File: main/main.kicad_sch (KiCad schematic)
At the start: 3 parts, among them SW1 SW_DPST_x2

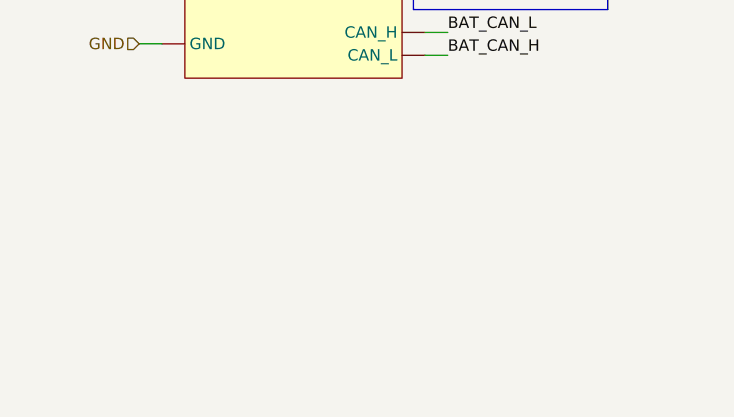
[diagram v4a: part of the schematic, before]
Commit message: Added motor, smart shunt, emergency switch and symbol of Cerbo GX
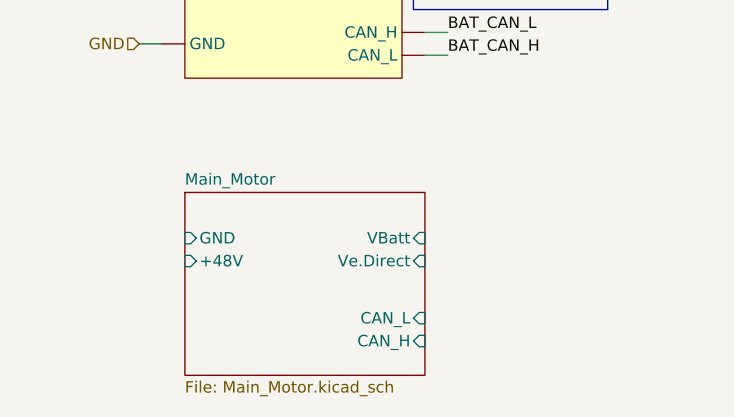
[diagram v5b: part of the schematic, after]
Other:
- added sheet Main_Motor (Main_Motor.kicad_sch)
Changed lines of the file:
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@@
+	)
+	(sheet
+		(at 29.21 125.73)
+		(size 26.67 20.32)
+		(fields_autoplaced yes)
+		(stroke
+			(width 0.1524)
+			(type solid)
+		)
+		(fill
+			(color 0 0 0 0.0000)
+		)
+		(property "Sheetname" "Main_Motor"
+			(at 29.21 125.0184 0)
+			(effects
+				(font
+					(size 1.27 1.27)
+				)
+				(justify left bottom)
+			)
+		)
+		(property "Sheetfile" "Main_Motor.kicad_sch"
+			(at 29.21 146.6346 0)
+			(effects
+				(font
+					(size 1.27 1.27)
+				)
+				(justify left top)
+			)
+		)
+		(pin "GND" input
+			(at 29.21 130.81 180)
+			(effects
+				(font
+					(size 1.27 1.27)
+				)
+				(justify left)
+			)
+		)
+		(pin "+48V" input
+			(at 29.21 133.35 180)
+			(effects
+				(font
+					(size 1.27 1.27)
+				)
+				(justify left)
+			)
+		)
+		(pin "VBatt" input
+			(at 55.88 130.81 0)
+			(effects
+				(font
+					(size 1.27 1.27)
+				)
+				(justify right)
+			)
+		)
+		(pin "Ve.Direct" input
+			(at 55.88 133.35 0)
+			(effects
+				(font
+					(size 1.27 1.27)
+				)
+				(justify right)
+			)
+		)
+		(pin "CAN_L" input
+			(at 55.88 139.7 0)
+			(effects
+				(font
+					(size 1.27 1.27)
+				)
+				(justify right)
+			)
+		)
+		(pin "CAN_H" input
+			(at 55.88 142.24 0)
+			(effects
+				(font
+					(size 1.27 1.27)
+				)
+				(justify right)
+			)
+		)
+		(instances
+			(project "main"
+				(path "/54fbbba9-a737-4199-9a4b-f9fa49b3de5e"
+					(page "20")
+				)
+			)
+		)
 	)
 	(sheet

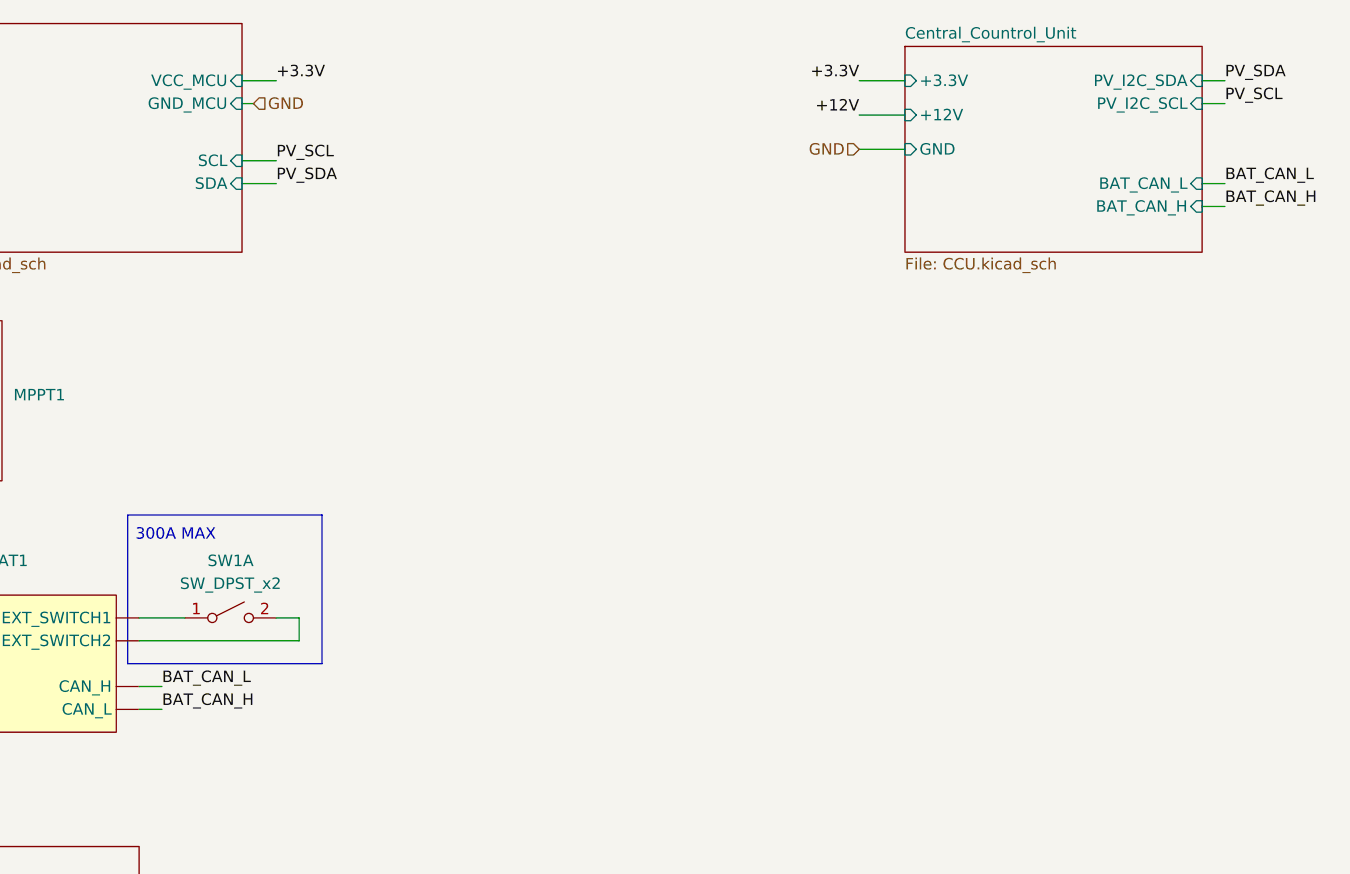
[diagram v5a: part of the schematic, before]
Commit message: Added sensors
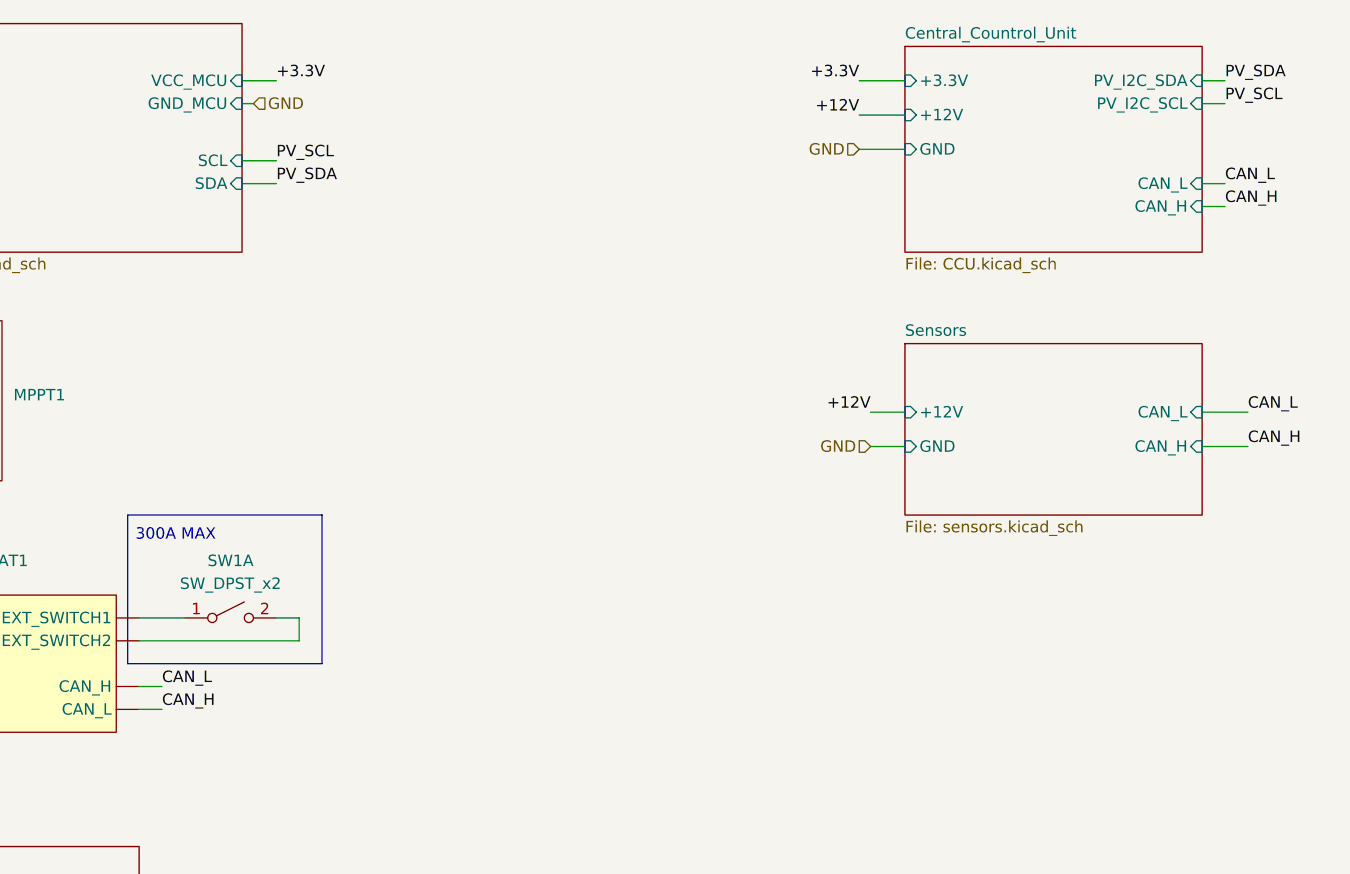
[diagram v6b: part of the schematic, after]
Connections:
- net BAT_CAN_H is gone; now on net GND: BAT1. (GND)
- net BAT_CAN_L is gone; now on net GND: BAT1. (GND)
- new net CAN_H: BAT1. (GND)
- new net CAN_L: BAT1. (GND)
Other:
- added sheet Sensors (sensors.kicad_sch)
- sheet Central_Countrol_Unit ports: added CAN_H, CAN_L; removed BAT_CAN_H, BAT_CAN_L
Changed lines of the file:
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@@
+	(wire
+		(pts
+			(xy 173.99 81.28) (xy 179.07 81.28)
+		)
+		(stroke
+			(width 0)
+			(type default)
+		)
+	)
 	(wire
 		(pts
@@
 		(pts
 			(xy 24.13 102.87) (xy 26.67 102.87)
+		)
+		(stroke
+			(width 0)
+			(type default)
+		)
+	)
+	(wire
+		(pts
+			(xy 137.16 77.47) (xy 140.97 77.47)
+		)
+		(stroke
+			(width 0)
+			(type default)
+		)
+	)
+	(wire
+		(pts
+			(xy 137.16 81.28) (xy 140.97 81.28)
+		)
+		(stroke
+			(width 0)
+			(type default)
+		)
+	)
+	(wire
+		(pts
+			(xy 173.99 77.47) (xy 179.07 77.47)
 		)
 		(stroke
@@
 		)
 	)
-	(label "BAT_CAN_H"
+	(label "CAN_H"
 		(at 176.53 54.61 0)
 		(fields_autoplaced yes)
@@
 		)
 	)
-	(label "BAT_CAN_L"
+	(label "+12V"
+		(at 137.16 77.47 180)
+		(fields_autoplaced yes)
+		(effects
+			(font
+				(size 1.27 1.27)
+			)
+			(justify right bottom)
+		)
+	)
+	(label "CAN_L"
+		(at 179.07 77.47 0)
+		(fields_autoplaced yes)
+		(effects
+			(font
+				(size 1.27 1.27)
+			)
+			(justify left bottom)
+		)
+	)
+	(label "CAN_H"
+		(at 179.07 81.28 0)
+		(fields_autoplaced yes)
+		(effects
+			(font
+				(size 1.27 1.27)
+			)
+			(justify left bottom)
+		)
+	)
+	(label "CAN_L"
 		(at 176.53 52.07 0)
 		(fields_autoplaced yes)
@@
 		)
 	)
-	(label "BAT_CAN_H"
+	(label "CAN_H"
 		(at 58.42 110.49 0)
 		(fields_autoplaced yes)
@@
 		)
 	)
-	(label "BAT_CAN_L"
+	(label "CAN_L"
 		(at 58.42 107.95 0)
 		(fields_autoplaced yes)
@@
 		(shape input)
 		(at 22.86 72.39 180)
+		(fields_autoplaced yes)
+		(effects
+			(font
+				(size 1.27 1.27)
+			)
+			(justify right)
+		)
+	)
+	(hierarchical_label "GND"
+		(shape input)
+		(at 137.16 81.28 180)
 		(fields_autoplaced yes)
 		(effects
@@
 			)
 		)
-		(pin "BAT_CAN_L" input
+		(pin "CAN_L" input
 			(at 173.99 52.07 0)
 			(effects
@@
 			)
 		)
-		(pin "BAT_CAN_H" input
+		(pin "CAN_H" input
 			(at 173.99 54.61 0)
 			(effects
@@
 				)
 			)
+		)
+	)
+	(sheet
+		(at 140.97 69.85)
+		(size 33.02 19.05)
+		(fields_autoplaced yes)
+		(stroke
+			(width 0.1524)
+			(type solid)
+		)
+		(fill
+			(color 0 0 0 0.0000)
+		)
+		(property "Sheetname" "Sensors"
+			(at 140.97 69.1384 0)
+			(effects
+				(font
+					(size 1.27 1.27)
+				)
+				(justify left bottom)
+			)
+		)
+		(property "Sheetfile" "sensors.kicad_sch"
+			(at 140.97 89.4846 0)
+			(effects
+				(font
+					(size 1.27 1.27)
+				)
+				(justify left top)
+			)
+		)
+		(pin "CAN_H" input
+			(at 173.99 81.28 0)
+			(effects
+				(font
+					(size 1.27 1.27)
+				)
+				(justify right)
+			)
+		)
+		(pin "CAN_L" input
+			(at 173.99 77.47 0)
+			(effects
+				(font
+					(size 1.27 1.27)
+				)
+				(justify right)
+			)
+		)
+		(pin "+12V" input
+			(at 140.97 77.47 180)
+			(effects
+				(font
+					(size 1.27 1.27)
+				)
+				(justify left)
+			)
+		)
+		(pin "GND" input
+			(at 140.97 81.28 180)
+			(effects
+				(font
+					(size 1.27 1.27)
+				)
+				(justify left)
+			)
+		)
+		(instances
+			(project "main"
+				(path "/54fbbba9-a737-4199-9a4b-f9fa49b3de5e"
+					(page "21")
+				)
+			)

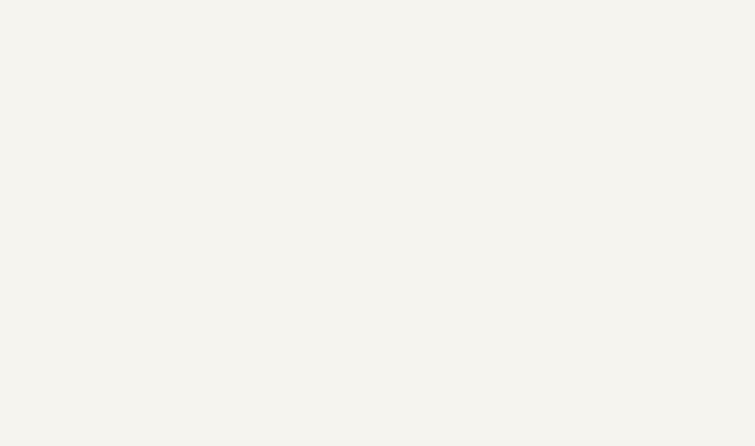
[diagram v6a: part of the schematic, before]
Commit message: Added control motor module
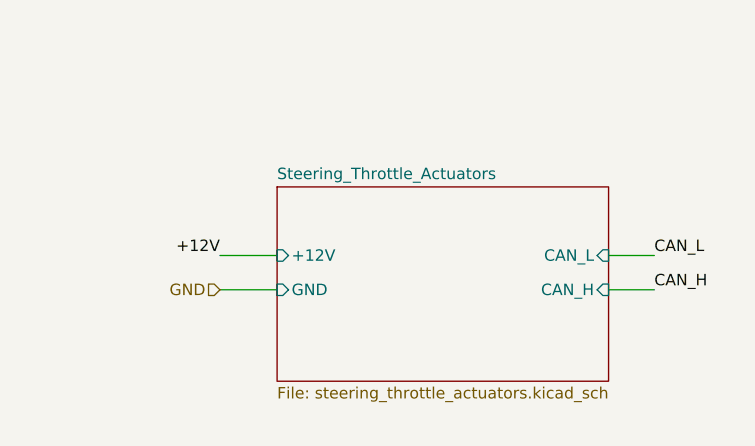
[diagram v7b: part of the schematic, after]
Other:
- added sheet Steering_Throttle_Actuators (steering_throttle_actuators.kicad_sch)
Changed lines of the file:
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@@
+	(wire
+		(pts
+			(xy 173.99 133.35) (xy 179.07 133.35)
+		)
+		(stroke
+			(width 0)
+			(type default)
+		)
+	)
 	(wire
 		(pts
@@
 	(wire
 		(pts
+			(xy 173.99 129.54) (xy 179.07 129.54)
+		)
+		(stroke
+			(width 0)
+			(type default)
+		)
+	)
+	(wire
+		(pts
 			(xy 55.88 107.95) (xy 58.42 107.95)
 		)
@@
 	(wire
 		(pts
+			(xy 130.81 133.35) (xy 137.16 133.35)
+		)
+		(stroke
+			(width 0)
+			(type default)
+		)
+	)
+	(wire
+		(pts
 			(xy 24.13 102.87) (xy 26.67 102.87)
 		)
@@
 		(pts
 			(xy 24.13 109.22) (xy 26.67 109.22)
+		)
+		(stroke
+			(width 0)
+			(type default)
+		)
+	)
+	(wire
+		(pts
+			(xy 130.81 129.54) (xy 137.16 129.54)
 		)
 		(stroke
@@
 	)
 	(label "+12V"
+		(at 130.81 129.54 180)
+		(fields_autoplaced yes)
+		(effects
+			(font
+				(size 1.27 1.27)
+			)
+			(justify right bottom)
+		)
+	)
+	(label "+12V"
 		(at 24.13 100.33 180)
 		(fields_autoplaced yes)
@@
 		)
 	)
+	(label "CAN_H"
+		(at 179.07 133.35 0)
+		(fields_autoplaced yes)
+		(effects
+			(font
+				(size 1.27 1.27)
+			)
+			(justify left bottom)
+		)
+	)
 	(label "PV_SDA"
 		(at 71.12 52.07 0)
@@
 	(label "CAN_H"
 		(at 179.07 81.28 0)
+		(fields_autoplaced yes)
+		(effects
+			(font
+				(size 1.27 1.27)
+			)
+			(justify left bottom)
+		)
+	)
+	(label "CAN_L"
+		(at 179.07 129.54 0)
 		(fields_autoplaced yes)
 		(effects
@@
 		(shape input)
 		(at 22.86 82.55 180)
+		(fields_autoplaced yes)
+		(effects
+			(font
+				(size 1.27 1.27)
+			)
+			(justify right)
+		)
+	)
+	(hierarchical_label "GND"
+		(shape input)
+		(at 130.81 133.35 180)
 		(fields_autoplaced yes)
 		(effects
@@
 				)
 			)
+		)
+	)
+	(sheet
+		(at 137.16 121.92)
+		(size 36.83 21.59)
+		(fields_autoplaced yes)
+		(stroke
+			(width 0.1524)
+			(type solid)
+		)
+		(fill
+			(color 0 0 0 0.0000)
+		)
+		(property "Sheetname" "Steering_Throttle_Actuators"
+			(at 137.16 121.2084 0)
+			(effects
+				(font
+					(size 1.27 1.27)
+				)
+				(justify left bottom)
+			)
+		)
+		(property "Sheetfile" "steering_throttle_actuators.kicad_sch"
+			(at 137.16 144.0946 0)
+			(effects
+				(font
+					(size 1.27 1.27)
+				)
+				(justify left top)
+			)
+		)
+		(pin "CAN_L" input
+			(at 173.99 129.54 0)
+			(effects
+				(font
+					(size 1.27 1.27)
+				)
+				(justify right)
+			)
+		)
+		(pin "+12V" input
+			(at 137.16 129.54 180)
+			(effects
+				(font
+					(size 1.27 1.27)
+				)
+				(justify left)
+			)
+		)
+		(pin "GND" input
+			(at 137.16 133.35 180)
+			(effects
+				(font
+					(size 1.27 1.27)
+				)
+				(justify left)
+			)
+		)
+		(pin "CAN_H" input
+			(at 173.99 133.35 0)
+			(effects
+				(font
+					(size 1.27 1.27)
+				)
+				(justify right)
+			)
+		)
+		(instances
+			(project "main"
+				(path "/54fbbba9-a737-4199-9a4b-f9fa49b3de5e"
+					(page "30")
+				)
+			)

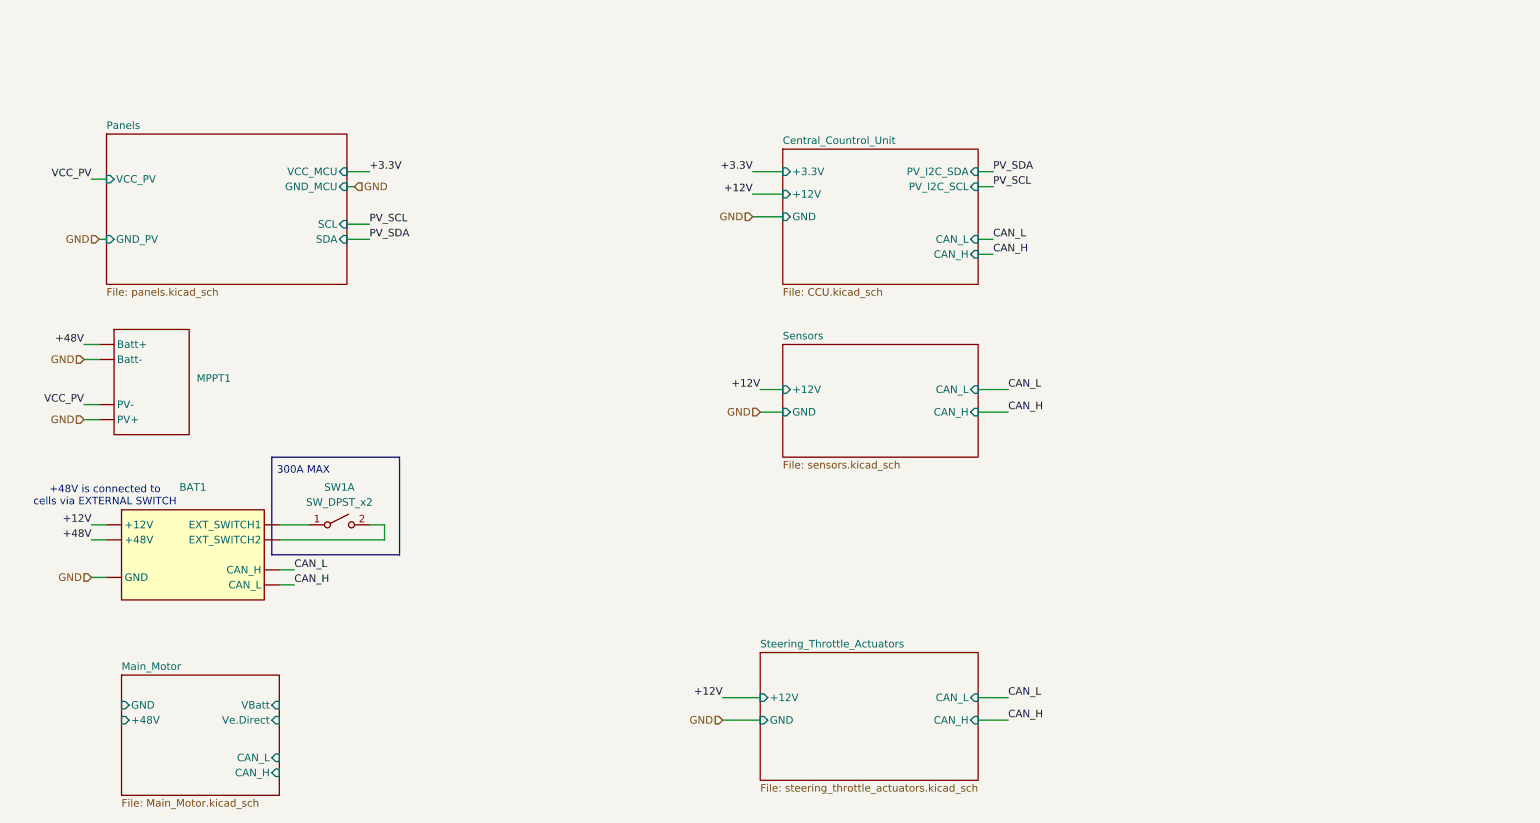
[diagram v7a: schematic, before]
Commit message: added cerbo gx and user interface sheet
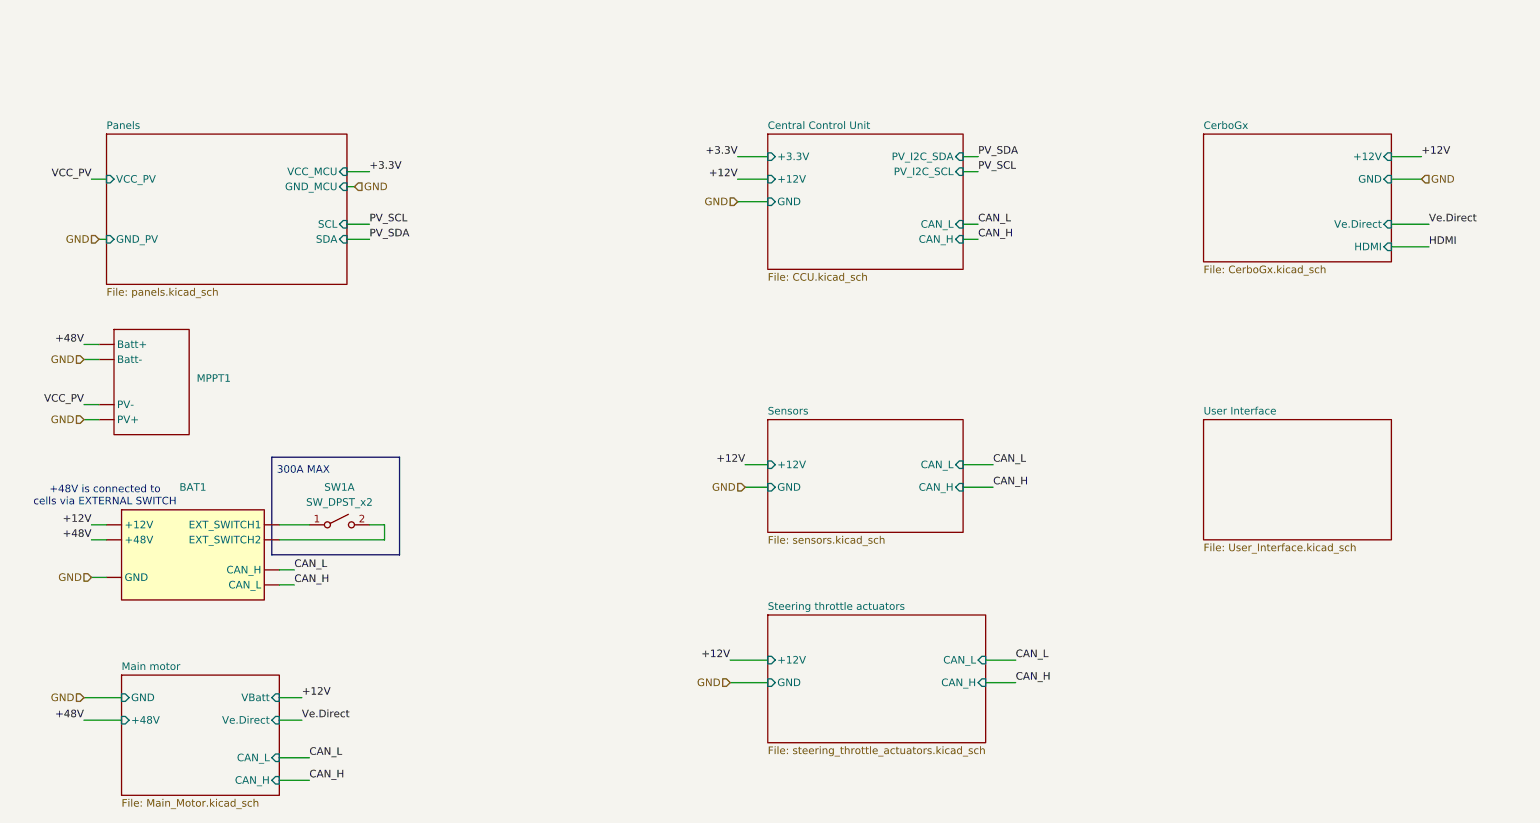
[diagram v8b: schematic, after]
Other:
- sheet Central_Countrol_Unit renamed Central Control Unit
- sheet Main_Motor renamed Main motor
- sheet Steering_Throttle_Actuators renamed Steering throttle actuators
- added sheet CerboGx (CerboGx.kicad_sch)
- added sheet User Interface (User_Interface.kicad_sch)
